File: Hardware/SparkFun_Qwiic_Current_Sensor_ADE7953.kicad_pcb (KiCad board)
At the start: 2 copper layers, 25.4 x 25.4 mm, 67 parts, among them J1 Qwiic_RA, J2 Qwiic_RA, J3 Conn_01x06, Q1 BSS138, Q2 BSS138, U5 AP3012

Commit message: Updated PCB and Schematic
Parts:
- removed C1, C2: 1.0uF, SparkFun-Capacitor:C_0603_1608Metric
- removed D2: PMEG4005EJ, SparkFun-Semiconductor-Standard:SOD-323
- removed JP2: I2C, SparkFun-Jumper:Jumper_3_NC-2_Trace
- removed JP3: LOGIC, SparkFun-Jumper:Jumper_3_NC-1_Trace
- removed JP4: I2C HV, SparkFun-Jumper:Jumper_3_NC-2_Trace
- removed L1: 10uH, SparkFun-Capacitor:C_0805_2012Metric
- removed Q1, Q2: BSS138, SparkFun-Semiconductor-Standard:SOT23-3
- removed R6: 100k, SparkFun-Resistor:R_0603_1608Metric
- removed R7, R8: 2.2k, SparkFun-Resistor:R_0603_1608Metric
- removed TP1, TP2: 1.0mm, SparkFun-Connector:TestPoint-1.0mm
- removed U5: AP3012, SparkFun-Semiconductor-Standard:SOT23-5
- removed kibuzzard-689A66F9: G***, kibuzzard-689A66F9
- removed kibuzzard-689A66FE: G***, kibuzzard-689A66FE
- removed kibuzzard-689A6706: G***, kibuzzard-689A6706
- added C10: 10uF, SparkFun-Capacitor:C_0603_1608Metric, F.Cu at (151.8, 106.2)
- added C3: 0.1uF, SparkFun-Capacitor:C_0603_1608Metric, F.Cu at (151.8, 88.6)
- added C4: 4.7uF, SparkFun-Capacitor:C_0603_1608Metric, F.Cu at (151.8, 91.1)
- added C5: 0.1uF, SparkFun-Capacitor:C_0603_1608Metric, F.Cu at (151.8, 93.6)
- added C6: 4.7uF, SparkFun-Capacitor:C_0603_1608Metric, F.Cu at (151.8, 96.1)
- added C7: 0.1uF, SparkFun-Capacitor:C_0603_1608Metric, F.Cu at (151.8, 98.6)
- added C8: 4.7uF, SparkFun-Capacitor:C_0603_1608Metric, F.Cu at (151.8, 101.1)
- added C9: 0.1uF, SparkFun-Capacitor:C_0603_1608Metric, F.Cu at (151.8, 103.6)
- added J4: Conn_01x04, SparkFun-Connector:1x04_P2.54mm, F.Cu at (132.5, 86.7)
- added J5: 3.5mm TRRS, SparkFun-Connector:Audio_Jack_3.5mm_TRRS_SMD_RA, B.Cu at (136.3, 92.4)
- added kibuzzard-69F8C31E: G***, kibuzzard-69F8C31E, F.Cu at (139.8, 106.4)
- added kibuzzard-69F8C32F: G***, kibuzzard-69F8C32F, B.Cu at (142.3, 107.3)
- added kibuzzard-69F8C340: G***, kibuzzard-69F8C340, F.Cu at (142.3, 107.3)
- added kibuzzard-69F8C396: G***, kibuzzard-69F8C396, F.Cu at (132.5, 88.6)
- added kibuzzard-69F8C3B2: G***, kibuzzard-69F8C3B2, F.Cu at (135.0, 88.6)
- added kibuzzard-69F8C3BE: G***, kibuzzard-69F8C3BE, F.Cu at (137.6, 88.6)
- added kibuzzard-69F8C3CC: G***, kibuzzard-69F8C3CC, F.Cu at (140.1, 88.6)
- R1: value 100k -> 4.7k
- R2: value 33k -> 4.7k
- R4, R5: value 2.2k -> 4.7k
- moved R4 27.0 mm to (156.6, 94.9)
- moved R5 21.7 mm to (156.6, 98.0)
- moved R1 21.3 mm to (156.6, 88.9)
- moved R2 21.3 mm to (156.6, 90.5)
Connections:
- J1 pad 2: 3.3V -> VDD
- J2 pad 2: 3.3V -> VDD
- J3 pad 2: 3.3V -> VDD
- J3 pad 3: HV_SDA -> SDA
- J3 pad 4: HV_SCL -> SCL
- J3 pad 5: 5V -> ~{RST}
- J3 pad 6: ~{SHDN} -> ~{INT}
- JP1 pad 2: 3.3V -> VDD
- R1 pad 1: Net-(U5-FB) -> A-
- R1 pad 2: 5V -> A+
- R2 pad 1: Net-(U5-FB) -> B-
- R2 pad 2: GND -> B+
- R4 pad 1: SDA -> SCL
- R4 pad 2: Net-(JP2-C) -> VDD
- R5 pad 1: Net-(JP2-A) -> SDA
- R5 pad 2: SCL -> VDD

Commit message: Updated PCB Layout
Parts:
- removed C10: 10uF, SparkFun-Capacitor:C_0603_1608Metric
- removed C5, C7, C9: 0.1uF, SparkFun-Capacitor:C_0603_1608Metric
- removed C6, C8: 4.7uF, SparkFun-Capacitor:C_0603_1608Metric
- removed kibuzzard-689A6411: G***, kibuzzard-689A6411
- removed kibuzzard-689A6418: G***, kibuzzard-689A6418
- removed kibuzzard-689A648B: G***, kibuzzard-689A648B
- removed kibuzzard-689A6494: G***, kibuzzard-689A6494
- removed kibuzzard-689A649F: G***, kibuzzard-689A649F
- removed kibuzzard-689A64A8: G***, kibuzzard-689A64A8
- removed kibuzzard-69F8C31E: G***, kibuzzard-69F8C31E
- removed kibuzzard-69F8C396: G***, kibuzzard-69F8C396
- removed kibuzzard-69F8C3B2: G***, kibuzzard-69F8C3B2
- removed kibuzzard-69F8C3BE: G***, kibuzzard-69F8C3BE
- removed kibuzzard-69F8C3CC: G***, kibuzzard-69F8C3CC
- added C1: 1.0uF, SparkFun-Capacitor:C_0402_1005Metric, F.Cu at (134.7, 98.4)
- added C2: 1.0uF, SparkFun-Capacitor:C_0402_1005Metric, F.Cu at (139.8, 102.2)
- added J6: Conn_01x02, SparkFun-Connector:1x02_P2.54mm, F.Cu at (129.6, 89.2)
- added JP2: ~, SparkFun-Jumper:Jumper_3_NC-2_Trace, B.Cu at (132.2, 103.8)
- added U1: ADE7953ACPZ, SparkFun-Semiconductor-Standard:QFN-28-1EP_4x4mm_P0.4mm_EP2.6x2.6mm, F.Cu at (136.0, 101.9)
- added kibuzzard-69F8FC1F: G***, kibuzzard-69F8FC1F, F.Cu at (131.5, 86.7)
- added kibuzzard-69F8FC1F: G***, kibuzzard-69F8FC1F, F.Cu at (140.3, 89.6)
- added kibuzzard-69F8FC56: G***, kibuzzard-69F8FC56, F.Cu at (140.2, 86.7)
- added kibuzzard-69F8FC56: G***, kibuzzard-69F8FC56, F.Cu at (131.5, 89.5)
- added kibuzzard-69F8FCF4: G***, kibuzzard-69F8FCF4, F.Cu at (142.3, 91.4)
- added kibuzzard-69F8FD80: G***, kibuzzard-69F8FD80, F.Cu at (129.6, 91.4)
- added kibuzzard-69F91A08: G***, kibuzzard-69F91A08, F.Cu at (139.8, 107.3)
- added kibuzzard-69F91BBC: G***, kibuzzard-69F91BBC, F.Cu at (158.2, 100.0)
- added kibuzzard-69F91C85: G***, kibuzzard-69F91C85, F.Cu at (158.2, 101.6)
- C3: value 0.1uF -> 1.0uF; footprint SparkFun-Capacitor:C_0603_1608Metric -> SparkFun-Capacitor:C_0402_1005Metric
- C4: value 4.7uF -> 1.0uF; footprint SparkFun-Capacitor:C_0603_1608Metric -> SparkFun-Capacitor:C_0402_1005Metric
- J4: value Conn_01x04 -> Conn_01x02; footprint SparkFun-Connector:1x04_P2.54mm -> SparkFun-Connector:1x02_P2.54mm
- J5: moved to F.Cu
- R1, R2: value 4.7k -> 100; footprint SparkFun-Resistor:R_0603_1608Metric -> SparkFun-Resistor:R_0402_1005Metric
- R4, R5: value 4.7k -> 2.2k; footprint SparkFun-Resistor:R_0603_1608Metric -> SparkFun-Resistor:R_0402_1005Metric
- moved R2 27.1 mm to (129.6, 93.0), turned to 0 degrees
- moved R5 22.4 mm to (136.0, 106.7)
- moved C3 22.3 mm to (132.5, 99.7), turned to 90 degrees
- moved C4 22.0 mm to (132.5, 101.6), turned to 90 degrees
- moved R4 21.6 mm to (138.5, 106.7), turned to -90 degrees
- moved G*** 19.4 mm to (145.5, 102.9)
- moved R1 14.9 mm to (142.3, 93.0)
- moved J4 10.2 mm to (142.3, 89.2), turned to 90 degrees
- moved J5 2.24 mm to (136.0, 90.2), turned to -90 degrees
- moved G*** 2.22 mm to (130.6, 100.3)
- moved JP1 0.32 mm to (129.6, 103.8)
- moved G*** 0.32 mm to (135.6, 98.1)
- moved kibuzzard-689A644B 0.31 mm to (136.0, 88.6)
- moved kibuzzard-689A642E 0.16 mm to (129.3, 102.9)
- moved G*** 0.06 mm to (136.0, 95.8)
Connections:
- C3 pad 1: Net-(IC1-VINTD) -> VINTA
- C4 pad 1: Net-(IC1-VINTD) -> 3.3V
- J1 pad 2: VDD -> 3.3V
- J2 pad 2: VDD -> 3.3V
- J3 pad 2: VDD -> 3.3V
- JP1 pad 2: VDD -> 3.3V
- R4 pad 2: VDD -> Net-(JP2-C)
- R5 pad 2: VDD -> Net-(JP2-A)
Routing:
- net 3.3V: track 0.00 -> 54.5 mm, vias 0 -> 4
- net A-: track 0.00 -> 37.1 mm, vias 0 -> 2
- net SCL: track 0.00 -> 36.0 mm, vias 0 -> 3
- net SDA: track 0.00 -> 32.7 mm, vias 0 -> 3
- net GND: track 0.00 -> 20.0 mm, vias 0 -> 6
- net B-: track 0.00 -> 19.6 mm
- net A+: track 0.00 -> 18.0 mm
- net B+: track 0.00 -> 16.4 mm
- net ~{INT}: track 0.00 -> 11.5 mm, vias 0 -> 2
- net Net-(JP2-C): track 0.00 -> 9.90 mm, vias 0 -> 1
- net ~{RST}: track 0.00 -> 7.94 mm
- net Net-(JP2-A): track 0.00 -> 6.76 mm, vias 0 -> 1
- net Net-(JP1-A): track 0.00 -> 2.53 mm, vias 0 -> 1
- net Net-(D1-A): track 0.00 -> 2.27 mm
- net VINTA: track 0.00 -> 1.78 mm
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
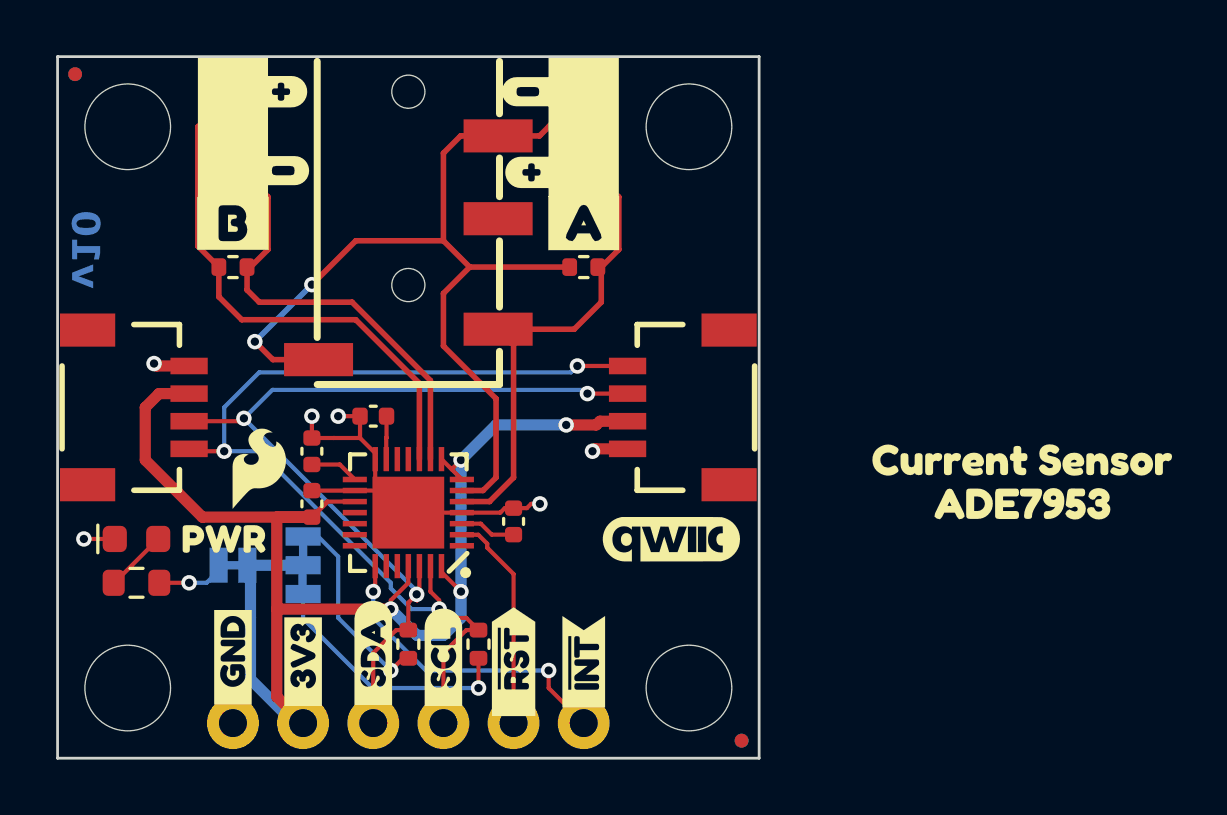
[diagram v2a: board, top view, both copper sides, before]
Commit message: Added silkscreen and minor alignment fixes
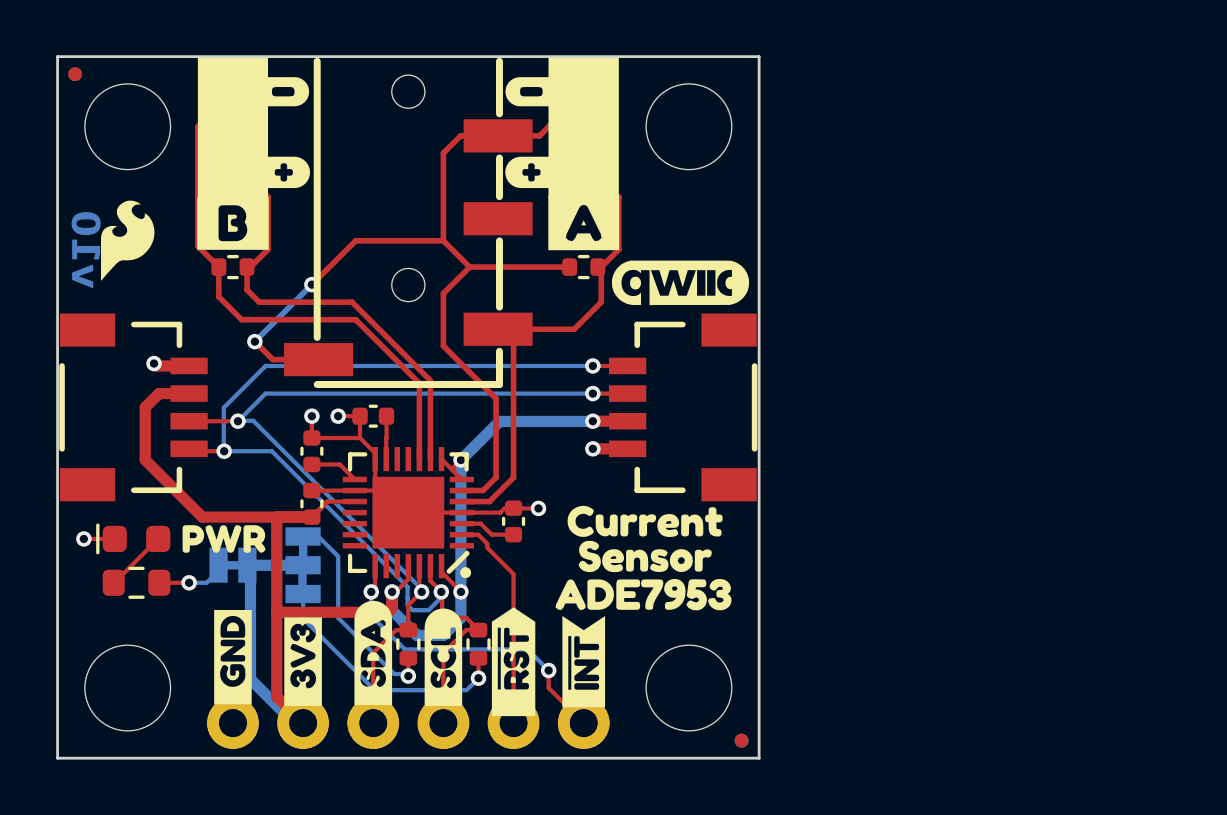
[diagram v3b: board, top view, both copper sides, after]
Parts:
- removed kibuzzard-689A644B: G***, kibuzzard-689A644B
- removed kibuzzard-689A6454: G***, kibuzzard-689A6454
- removed kibuzzard-689A6479: G***, kibuzzard-689A6479
- removed kibuzzard-689A6481: G***, kibuzzard-689A6481
- removed kibuzzard-689A670C: G***, kibuzzard-689A670C
- removed kibuzzard-689A6759: G***, kibuzzard-689A6759
- removed kibuzzard-689A6762: G***, kibuzzard-689A6762
- removed kibuzzard-689A676B: G***, kibuzzard-689A676B
- removed kibuzzard-689A6771: G***, kibuzzard-689A6771
- removed kibuzzard-689A6775: G***, kibuzzard-689A6775
- removed kibuzzard-69F8C32F: G***, kibuzzard-69F8C32F
- removed kibuzzard-69F91BBC: G***, kibuzzard-69F91BBC
- removed kibuzzard-69F91C85: G***, kibuzzard-69F91C85
- added kibuzzard-69FA128B: G***, kibuzzard-69FA128B, F.Cu at (144.5, 104.9)
- added kibuzzard-69FA128B: G***, kibuzzard-69FA128B, B.Cu at (135.6, 100.6)
- added kibuzzard-69FA1293: G***, kibuzzard-69FA1293, F.Cu at (144.5, 102.2)
- added kibuzzard-69FA1293: G***, kibuzzard-69FA1293, B.Cu at (135.6, 97.8)
- added kibuzzard-69FA12A1: G***, kibuzzard-69FA12A1, F.Cu at (144.5, 103.5)
- added kibuzzard-69FA12A1: G***, kibuzzard-69FA12A1, B.Cu at (135.6, 99.1)
- added kibuzzard-69FA12DB: G***, kibuzzard-69FA12DB, B.Cu at (142.3, 107.3)
- added kibuzzard-69FA1306: G***, kibuzzard-69FA1306, B.Cu at (139.8, 107.2)
- added kibuzzard-69FA13A0: G***, kibuzzard-69FA13A0, B.Cu at (140.4, 86.7)
- added kibuzzard-69FA13AB: G***, kibuzzard-69FA13AB, B.Cu at (140.4, 89.2)
- added kibuzzard-69FA13C4: G***, kibuzzard-69FA13C4, B.Cu at (131.5, 86.7)
- added kibuzzard-69FA13D5: G***, kibuzzard-69FA13D5, B.Cu at (131.5, 89.2)
- added kibuzzard-69FA1766: G***, kibuzzard-69FA1766, B.Cu at (134.6, 103.9)
- moved G*** 9.53 mm to (125.8, 92.1)
- moved G*** 9.29 mm to (145.8, 93.6)
- moved G*** 4.07 mm to (136.0, 91.8)
- moved kibuzzard-69F8FC1F 2.92 mm to (131.6, 89.6)
- moved kibuzzard-69F8FC56 2.86 mm to (131.5, 86.7)
- moved G*** 2.59 mm to (135.6, 95.5)
- moved kibuzzard-689A6796 0.28 mm to (126.7, 103.8)
- moved kibuzzard-69F8FC56 0.13 mm to (140.3, 86.7)
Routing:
- net SCL: track 36.0 -> 36.7 mm
- net Net-(JP2-C): track 9.90 -> 9.21 mm
- net 3.3V: track 54.5 -> 55.1 mm
- net Net-(JP2-A): track 6.76 -> 7.30 mm

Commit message: Added XTAL Osc.
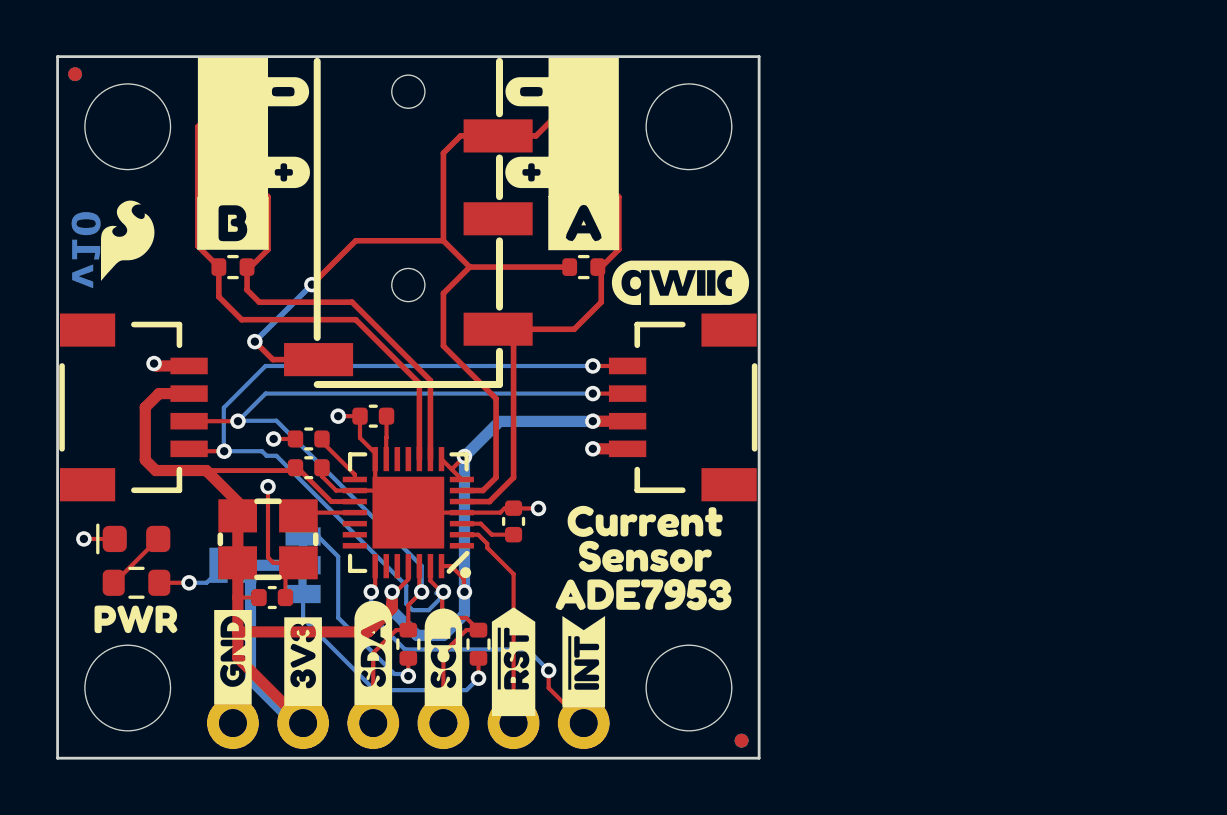
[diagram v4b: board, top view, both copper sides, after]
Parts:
- added C5: 1.0uF, SparkFun-Capacitor:C_0402_1005Metric, F.Cu at (131.0, 105.0)
- added Y1: 3.579MHz, SparkFun-Clock:Crystal_SMD_3.2x2.5mm, F.Cu at (130.9, 102.9)
- moved kibuzzard-689A642E 4.32 mm to (126.1, 105.8)
- moved C4 1.31 mm to (132.4, 100.3), turned to 0 degrees
- moved C3 0.46 mm to (132.4, 99.2), turned to 180 degrees
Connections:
- U1 pad 18: Net-(U1-CLKIN) -> CLKIN
- U1 pad 19: Net-(U1-CLKOUT) -> unconnected-(U1-CLKOUT-Pad19)
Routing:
- net 3.3V: track 55.1 -> 59.0 mm
- net GND: track 19.7 -> 23.4 mm, vias 6 -> 7
- net CLKIN: track 0.00 -> 2.09 mm
- net A-: track 37.1 -> 35.3 mm

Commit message: Fixed Reset Pin and Shunt Resistors
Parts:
- removed the G*** at (125.8, 92.1)
- removed the G*** at (135.6, 95.5)
- added C6: 33pF, SparkFun-Capacitor:C_0402_1005Metric, F.Cu at (145.4, 91.7)
- added C7: 33pF, SparkFun-Capacitor:C_0402_1005Metric, F.Cu at (142.1, 94.7)
- added C8: 33pF, SparkFun-Capacitor:C_0402_1005Metric, F.Cu at (129.6, 94.7)
- added C9: 33pF, SparkFun-Capacitor:C_0402_1005Metric, F.Cu at (126.4, 91.7)
- added G***: Flame, SparkFun-Aesthetic:SparkFun_Flame_4mm, F.Cu at (140.4, 99.1)
- added R10: 1k, SparkFun-Resistor:R_0402_1005Metric, F.Cu at (127.5, 91.7)
- added R6: 4.7k, SparkFun-Resistor:R_0402_1005Metric, F.Cu at (141.1, 102.2)
- added R7: 1k, SparkFun-Resistor:R_0402_1005Metric, F.Cu at (144.4, 91.7)
- added R8: 1k, SparkFun-Resistor:R_0402_1005Metric, F.Cu at (141.1, 94.7)
- added R9: 1k, SparkFun-Resistor:R_0402_1005Metric, F.Cu at (130.6, 94.7)
- added Ref**: Val**, SparkFun-Aesthetic:OSHW_Logo_4mm, B.Cu at (145.6, 104.0)
- R1, R2: value 100 -> 5.6; footprint SparkFun-Resistor:R_0402_1005Metric -> SparkFun-Resistor:R_0603_1608Metric
- moved G*** 4.44 mm to (136.0, 96.2)
- moved kibuzzard-69FA1293 1.00 mm to (136.6, 98.1)
- moved kibuzzard-69FA12A1 0.71 mm to (135.0, 99.4)
- moved kibuzzard-69FA128B 0.45 mm to (136.0, 101.0)
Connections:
- U1 pad 10: B- -> IBN
- U1 pad 5: A+ -> IAP
- U1 pad 6: A- -> IAN
- U1 pad 9: B+ -> IBP
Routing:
- net IBN: track 0.00 -> 17.3 mm
- net IAP: track 0.00 -> 13.6 mm
- net A-: track 35.3 -> 23.0 mm
- net IBP: track 0.00 -> 11.6 mm
- net B-: track 19.6 -> 8.13 mm
- net B+: track 16.4 -> 6.01 mm
- net IAN: track 0.00 -> 8.59 mm
- net A+: track 18.0 -> 12.8 mm, vias 0 -> 1
- net 3.3V: track 59.0 -> 63.3 mm
- net GND: track 23.4 -> 26.6 mm, vias 7 -> 11
- net ~{RST}: track 7.94 -> 9.86 mm

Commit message: Implemented changes after design review
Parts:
- removed the G*** at (145.8, 93.6)
- removed kibuzzard-69F91A08: G***, kibuzzard-69F91A08
- removed kibuzzard-69FA1306: G***, kibuzzard-69FA1306
- removed kibuzzard-69FA1766: G***, kibuzzard-69FA1766
- added G***: LOGO, SparkFun-Aesthetic:qwiic_4mm, F.Cu at (146.1, 93.7)
- added JP3: SCLK, SparkFun-Jumper:Jumper_3_NC-1_Trace, B.Cu at (142.6, 103.6)
- added JP4: CS, SparkFun-Jumper:Jumper_2_NC_Trace, B.Cu at (139.1, 102.9)
- added R11: 2.2k, SparkFun-Resistor:R_0402_1005Metric, F.Cu at (139.8, 104.5)
- added kibuzzard-69FCD097: G***, kibuzzard-69FCD097, B.Cu at (134.6, 103.9)
- added kibuzzard-69FCDE2E: G***, kibuzzard-69FCDE2E, B.Cu at (136.9, 102.6)
- added kibuzzard-69FCDE6F: G***, kibuzzard-69FCDE6F, B.Cu at (145.8, 103.8)
- added kibuzzard-69FD0DBC: G***, kibuzzard-69FD0DBC, B.Cu at (136.0, 87.9)
- added kibuzzard-69FD0DD3: G***, kibuzzard-69FD0DD3, B.Cu at (136.0, 88.9)
- added kibuzzard-69FD0DDA: G***, kibuzzard-69FD0DDA, B.Cu at (136.0, 89.9)
- added kibuzzard-69FD0F08: G***, kibuzzard-69FD0F08, B.Cu at (136.0, 90.8)
- added kibuzzard-69FD1032: G***, kibuzzard-69FD1032, F.Cu at (140.5, 93.3)
- added kibuzzard-69FD1060: G***, kibuzzard-69FD1060, F.Cu at (139.6, 93.4)
- added kibuzzard-69FD10A0: G***, kibuzzard-69FD10A0, F.Cu at (139.8, 107.0)
- added kibuzzard-69FD10AE: G***, kibuzzard-69FD10AE, B.Cu at (139.8, 107.0)
- JP2: value ~ -> I²C
- R6: footprint SparkFun-Resistor:R_0402_1005Metric -> SparkFun-Resistor:R_0603_1608Metric
- moved Ref** 11.0 mm to (145.2, 93.0)
- moved kibuzzard-69FA12A1 1.35 mm to (136.0, 98.4)
- moved kibuzzard-69FA1293 1.14 mm to (136.0, 97.2)
- moved kibuzzard-69FA128B 0.95 mm to (136.0, 100.0)
- moved G*** 0.63 mm to (136.0, 95.6)
- moved R8 0.32 mm to (141.4, 94.9)
- moved R6 0.31 mm to (141.0, 102.6)
- moved C7 0.29 mm to (142.3, 94.9)
- moved R9 0.23 mm to (130.6, 94.9)
- moved C8 0.23 mm to (129.6, 94.9)
- moved C5 0.19 mm to (131.2, 105.1)
- moved R7 0.12 mm to (144.5, 91.8)
- moved C6 0.09 mm to (145.5, 91.8)
- moved R10 0.08 mm to (127.4, 91.8)
- moved C9 0.05 mm to (126.4, 91.8)
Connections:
- J3 pad 5: ~{RST} -> ZX_I
- R6 pad 1: ~{RST} -> Net-(U1-~{RESET})
- U1 pad 2: ~{RST} -> Net-(U1-~{RESET})
- U1 pad 21: unconnected-(U1-ZX_I-Pad21) -> ZX_I
- U1 pad 25: 3.3V -> Net-(JP3-B)
- U1 pad 28: 3.3V -> Net-(JP4-A)
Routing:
- net ZX_I: track 0.00 -> 10.8 mm, vias 0 -> 1
- net Net-(JP3-B): track 0.00 -> 10.8 mm, vias 0 -> 1
- net ~{RST}: track 9.86 -> 0.00 mm
- net Net-(JP3-C): track 0.00 -> 6.51 mm, vias 0 -> 1
- net Net-(JP4-A): track 0.00 -> 3.86 mm, vias 0 -> 1
- net Net-(U1-~{RESET}): track 0.00 -> 3.46 mm
- net SDA: track 32.7 -> 35.2 mm
- net 3.3V: track 63.3 -> 64.6 mm
- net SCL: track 36.8 -> 37.6 mm
- net IBP: track 11.6 -> 12.4 mm
- net IBN: track 17.3 -> 18.1 mm
- net IAP: track 13.6 -> 14.3 mm
- net GND: track 26.6 -> 27.3 mm, vias 11 -> 16
- net Net-(JP2-C): track 9.21 -> 9.81 mm
- net A-: track 23.0 -> 23.6 mm
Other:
- board text added: "v01"
- board text removed: "v10"
